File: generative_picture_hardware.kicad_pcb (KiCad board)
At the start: 2 copper layers, 100 x 100 mm, 64 parts, among them J1 e_Paper_HAT, J2 Conn_ARM_JTAG_SWD_10, J3 USB_C_Receptacle_USB2.0, Q1 PMN48XP, Q2 DMG9926UDM, Q3 MBT3904DW1, SW1 SW_Push, SW2 SW_Push, U1 AP2112K-3.3, U2 ESP32-WROOM-32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

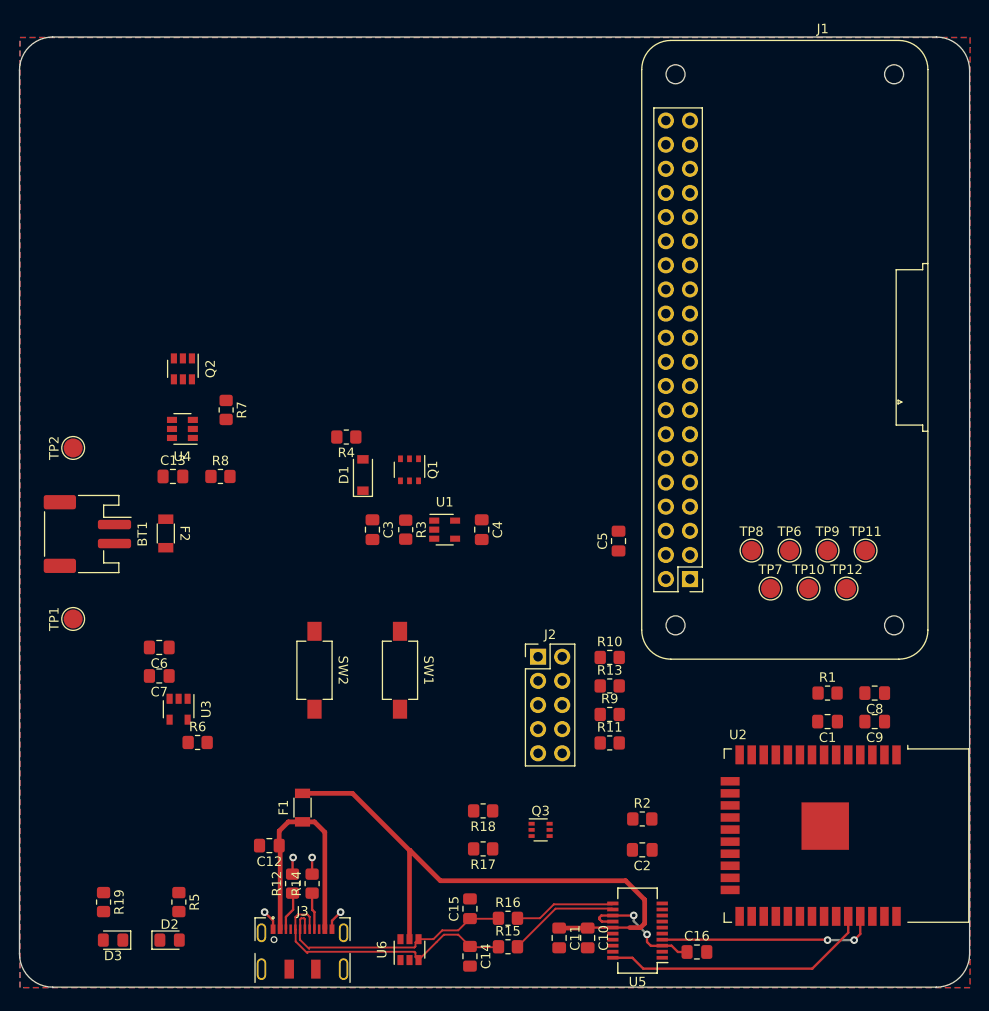
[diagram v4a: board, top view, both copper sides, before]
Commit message: Reroutes battery charging, protection and regulator
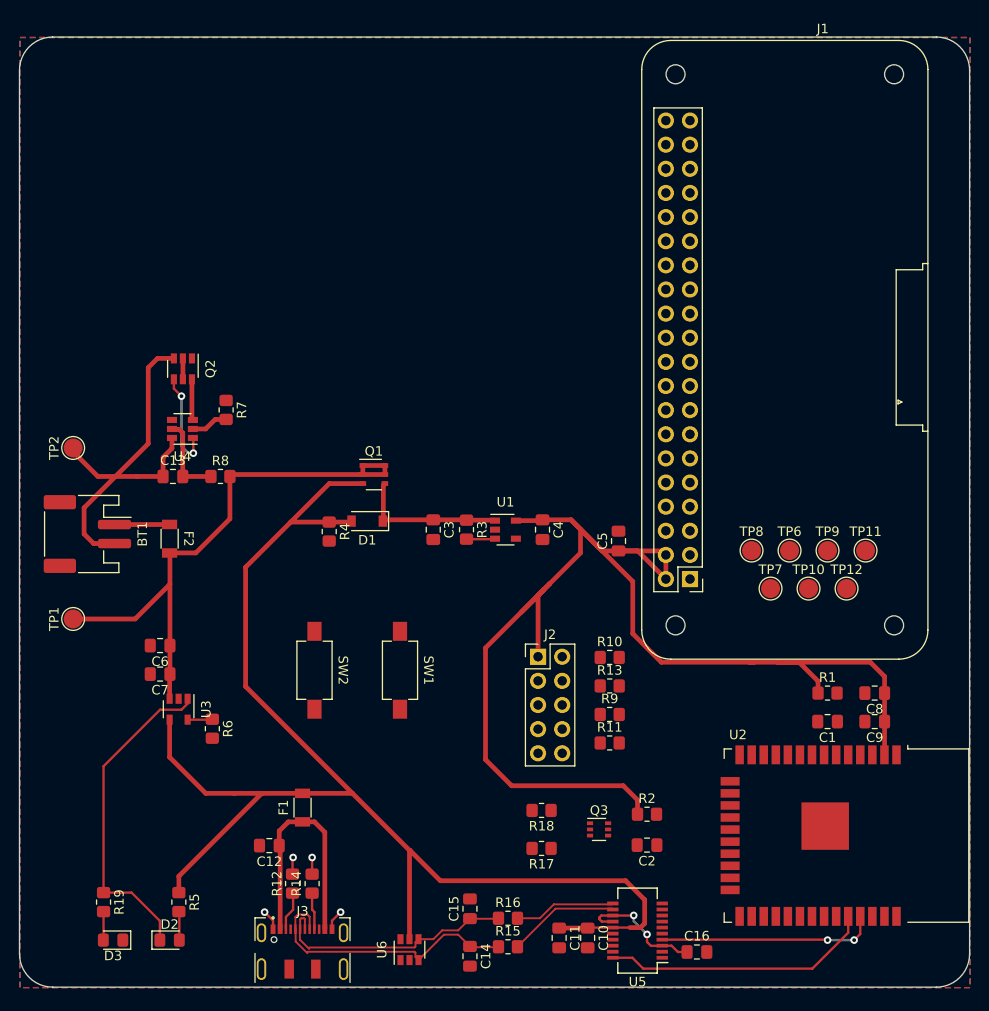
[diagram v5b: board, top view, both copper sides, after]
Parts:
- moved R4 10.1 mm to (132.6, 104.0), turned to -90 degrees
- moved C3 6.40 mm to (143.5, 103.8)
- moved C4 6.40 mm to (155.0, 103.8)
- moved R3 6.40 mm to (147.0, 103.8)
- moved U1 6.40 mm to (151.1, 103.8)
- moved R17 6.15 mm to (154.9, 137.3)
- moved R18 6.15 mm to (154.9, 133.3)
- moved Q3 6.15 mm to (160.9, 135.3)
- moved D1 4.87 mm to (136.6, 102.9), turned to 180 degrees
- moved Q1 3.78 mm to (137.2, 98.0), turned to 0 degrees
- moved R6 2.12 mm to (120.2, 124.8), turned to -90 degrees
- moved C2 0.71 mm to (166.0, 137.0)
- moved R2 0.71 mm to (166.0, 133.8)
- moved F2 0.68 mm to (115.8, 104.8)
- moved C6 0.22 mm to (114.8, 116.0)
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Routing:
- net +3V3: track 0.00 -> 144.1 mm
- net +5V: track 61.8 -> 146.4 mm
- net +BATT: track 0.00 -> 60.3 mm
- net Net-(BT1-Pad2): track 0.00 -> 42.4 mm
- net Net-(D2-Pad1): track 0.00 -> 34.6 mm
- net VCC: track 0.00 -> 15.9 mm
- net Net-(Q2-Pad4): track 0.00 -> 10.5 mm, vias 0 -> 2
- net Net-(C13-Pad2): track 0.00 -> 8.85 mm
- net Net-(BT1-Pad1): track 0.00 -> 5.80 mm
- net Net-(Q2-Pad6): track 0.00 -> 4.32 mm
- net Net-(R7-Pad2): track 0.00 -> 3.91 mm
- net Net-(D2-Pad2): track 0.00 -> 3.02 mm
- net Net-(R3-Pad2): track 0.00 -> 3.02 mm
- net Net-(D3-Pad2): track 0.00 -> 3.01 mm
- net Net-(R6-Pad1): track 0.00 -> 2.62 mm
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
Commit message: Reroutes the components that were left (except for GND)
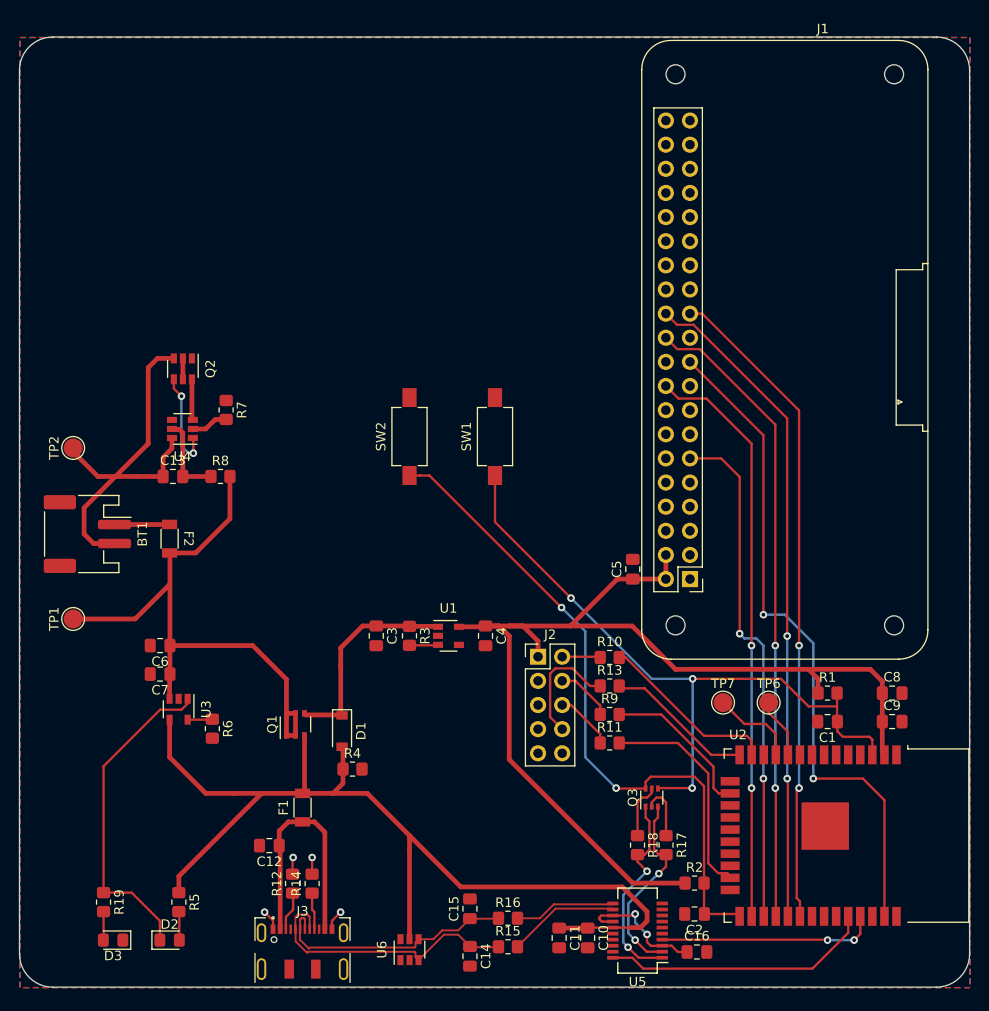
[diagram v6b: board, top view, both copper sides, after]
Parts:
- removed TP10: IO33, TestPoint:TestPoint_Pad_D2.0mm
- removed TP11: IO34, TestPoint:TestPoint_Pad_D2.0mm
- removed TP12: IO35, TestPoint:TestPoint_Pad_D2.0mm
- removed TP8: IO27, TestPoint:TestPoint_Pad_D2.0mm
- removed TP9: IO32, TestPoint:TestPoint_Pad_D2.0mm
- moved Q1 27.6 mm to (129.0, 124.3), turned to 90 degrees
- moved SW1 26.6 mm to (150.0, 94.0), turned to 90 degrees
- moved SW2 26.6 mm to (141.0, 94.0), turned to 90 degrees
- moved R4 25.1 mm to (135.0, 129.0), turned to 0 degrees
- moved D1 22.3 mm to (133.9, 125.0), turned to -90 degrees
- moved TP6 16.2 mm to (178.8, 122.0)
- moved R17 13.1 mm to (168.0, 137.0), turned to -90 degrees
- moved TP7 13.0 mm to (174.0, 122.0)
- moved C3 12.7 mm to (137.5, 115.0)
- moved C4 12.7 mm to (149.0, 115.0)
- moved R3 12.7 mm to (141.0, 115.0)
- moved U1 12.7 mm to (145.1, 115.0)
- moved R18 10.7 mm to (165.0, 137.0), turned to -90 degrees
- moved C2 8.81 mm to (171.0, 144.2)
- moved R2 8.81 mm to (171.0, 141.0)
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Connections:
- U2 pad 12: Net-(TP8-Pad1) -> unconnected-(U2-Pad12)
- U2 pad 6: Net-(TP11-Pad1) -> unconnected-(U2-Pad6)
- U2 pad 7: Net-(TP12-Pad1) -> unconnected-(U2-Pad7)
- U2 pad 8: Net-(TP9-Pad1) -> unconnected-(U2-Pad8)
- U2 pad 9: Net-(TP10-Pad1) -> unconnected-(U2-Pad9)
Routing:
- net ESP_EN: track 0.00 -> 73.8 mm, vias 0 -> 3
- net EPD_DIN: track 0.00 -> 71.2 mm, vias 0 -> 2
- net ESP_BOOT: track 0.00 -> 71.0 mm, vias 0 -> 2
- net EPD_CS: track 0.00 -> 69.8 mm, vias 0 -> 2
- net EPD_CLK: track 0.00 -> 69.2 mm, vias 0 -> 2
- net EPD_DC: track 0.00 -> 67.1 mm, vias 0 -> 2
- net EPD_BUSY: track 0.00 -> 61.3 mm, vias 0 -> 2
- net EPD_RST: track 0.00 -> 54.1 mm, vias 0 -> 2
- net +5V: track 146.4 -> 108.2 mm
- net +3V3: track 144.1 -> 116.7 mm
- net MTDO: track 0.00 -> 23.2 mm
- net DTR: track 0.00 -> 21.6 mm, vias 0 -> 2
- net RTS: track 0.00 -> 20.5 mm, vias 0 -> 2
- net MTMS: track 0.00 -> 19.1 mm
- net MTCK: track 0.00 -> 16.4 mm
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
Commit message: Routes all GND without relying on front copper fill
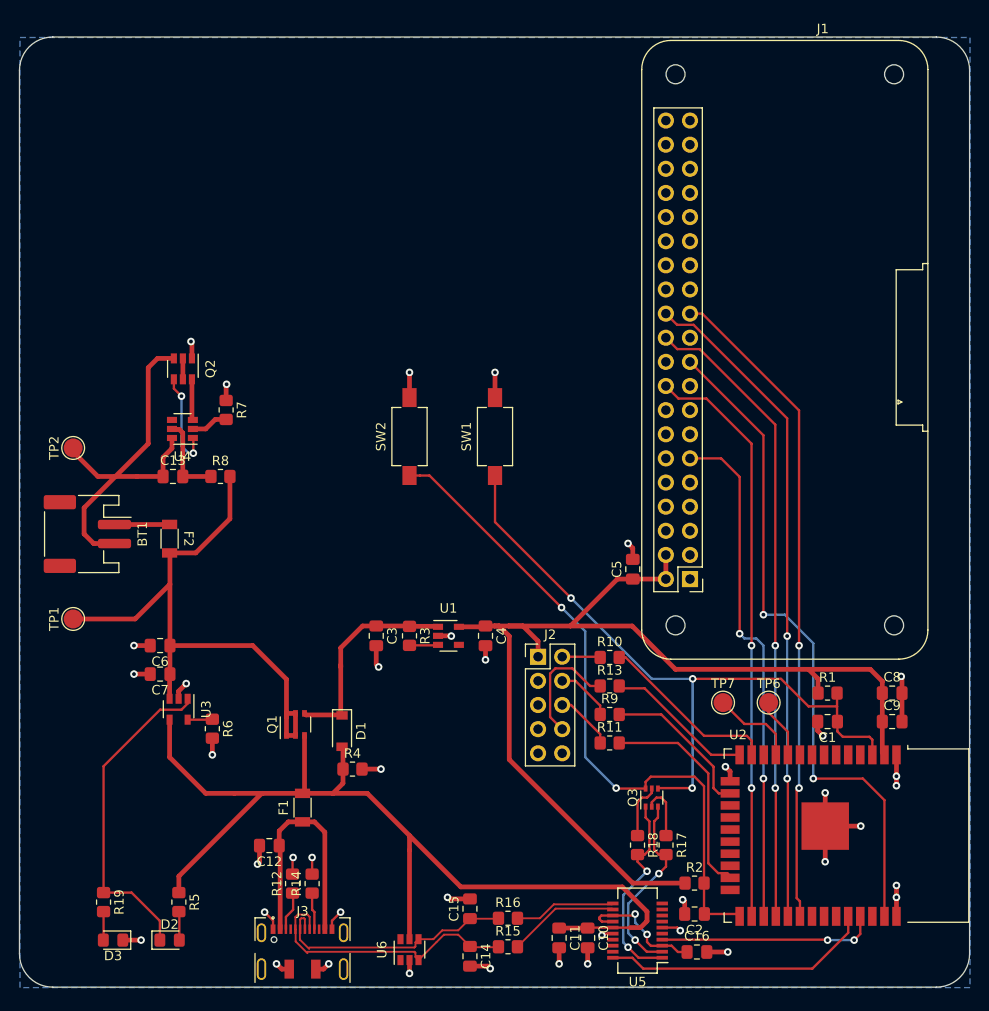
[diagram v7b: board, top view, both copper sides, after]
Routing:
- net GND: track 7.86 -> 82.3 mm, vias 4 -> 40
- removed copper zone on F.Cu, net GND
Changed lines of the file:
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@@
   (segment (start 115.74 103.26) (end 115.75 103.25) (width 0.5) (layer "F.Cu") (net 2))
   (segment (start 109.95 103.26) (end 115.74 103.26) (width 0.5) (layer "F.Cu") (net 2))
+  (segment (start 121.7 88.55) (end 121.75 88.5) (width 0.5) (layer "F.Cu") (net 3))
+  (segment (start 172.2875 148.25) (end 174.5 148.25) (width 0.5) (layer "F.Cu") (net 3))
+  (segment (start 192.255 141.255) (end 192.255 144.499748) (width 0.5) (layer "F.Cu") (net 3))
+  (segment (start 169.9625 142.9625) (end 169.75 142.75) (width 0.5) (layer "F.Cu") (net 3))
+  (segment (start 183.9625 124.9625) (end 184.5 125.5) (width 0.5) (layer "F.Cu") (net 3))
+  (segment (start 192.255 130.745) (end 192.255 127.499748) (width 0.5) (layer "F.Cu") (net 3))
+  (segment (start 184.755 134.999748) (end 184.755 138.745) (width 0.5) (layer "F.Cu") (net 3))
+  (segment (start 159.75 147.8075) (end 159.75 149.5) (width 0.5) (layer "F.Cu") (net 3))
+  (segment (start 188.499748 134.999748) (end 188.5 135) (width 0.5) (layer "F.Cu") (net 3))
   (segment (start 126.64 144.944098) (end 125.75 144.054098) (width 0.25) (layer "F.Cu") (net 3))
+  (segment (start 156.75 147.8075) (end 156.75 149.5) (width 0.5) (layer "F.Cu") (net 3))
   (segment (start 128.6925 138.361598) (end 128.75 138.304098) (width 0.25) (layer "F.Cu") (net 3))
   (segment (start 130.75 140.054098) (end 130.75 138.304098) (width 0.25) (layer "F.Cu") (net 3))
+  (segment (start 131.14 150.051598) (end 131.948402 150.051598) (width 0.5) (layer "F.Cu") (net 3))
+  (segment (start 141 89.9) (end 141 87.25) (width 0.5) (layer "F.Cu") (net 3))
+  (segment (start 150 89.9) (end 150 87.25) (width 0.5) (layer "F.Cu") (net 3))
+  (segment (start 164.5 106.925) (end 164.5 105.75) (width 0.5) (layer "F.Cu") (net 3))
+  (segment (start 162.4 146.3175) (end 161.4325 146.3175) (width 0.25) (layer "F.Cu") (net 3))
+  (segment (start 184.755 138.745) (end 184.75 138.75) (width 0.5) (layer "F.Cu") (net 3))
+  (segment (start 174.745 130.284748) (end 174.745 129.245) (width 0.5) (layer "F.Cu") (net 3))
+  (segment (start 127.551598 150.051598) (end 127 149.5) (width 0.5) (layer "F.Cu") (net 3))
+  (segment (start 147.3625 149.7375) (end 149.2375 149.7375) (width 0.5) (layer "F.Cu") (net 3))
+  (segment (start 169.9625 144.25) (end 169.9625 142.9625) (width 0.5) (layer "F.Cu") (net 3))
+  (segment (start 137.5 116.0125) (end 137.5 118) (width 0.5) (layer "F.Cu") (net 3))
+  (segment (start 118.1 85.775) (end 118.1 84.1) (width 0.5) (layer "F.Cu") (net 3))
+  (segment (start 147.3625 142.6625) (end 145.1625 142.6625) (width 0.5) (layer "F.Cu") (net 3))
+  (segment (start 110.825 147) (end 112.75 147) (width 0.5) (layer "F.Cu") (net 3))
+  (segment (start 131.948402 150.051598) (end 132.5 149.5) (width 0.5) (layer "F.Cu") (net 3))
+  (segment (start 169.1825 145.6825) (end 169.5 146) (width 0.25) (layer "F.Cu") (net 3))
+  (segment (start 145.4 115) (end 145.375 114.975) (width 0.5) (layer "F.Cu") (net 3))
+  (segment (start 136 129) (end 138 129) (width 0.5) (layer "F.Cu") (net 3))
+  (segment (start 141 149.102479) (end 141 150.5) (width 0.5) (layer "F.Cu") (net 3))
+  (segment (start 137.5 118) (end 137.75 118.25) (width 0.5) (layer "F.Cu") (net 3))
+  (segment (start 192.75 119.25) (end 192.8375 119.3375) (width 0.5) (layer "F.Cu") (net 3))
+  (segment (start 116.7 120.8) (end 117.5 120) (width 0.5) (layer "F.Cu") (net 3))
   (segment (start 132.84 144.964098) (end 133.75 144.054098) (width 0.25) (layer "F.Cu") (net 3))
+  (segment (start 121.7 90.2) (end 121.7 88.55) (width 0.5) (layer "F.Cu") (net 3))
+  (segment (start 125.2125 138.7875) (end 125 139) (width 0.5) (layer "F.Cu") (net 3))
+  (segment (start 128.34 150.051598) (end 127.551598 150.051598) (width 0.5) (layer "F.Cu") (net 3))
+  (segment (start 145.1625 142.6625) (end 145 142.5) (width 0.5) (layer "F.Cu") (net 3))
+  (segment (start 192.25 141.25) (end 192.255 141.255) (width 0.5) (layer "F.Cu") (net 3))
+  (segment (start 174.745 129.245) (end 174.25 128.75) (width 0.5) (layer "F.Cu") (net 3))
+  (segment (start 184.755 131.505) (end 184.75 131.5) (width 0.5) (layer "F.Cu") (net 3))
+  (segment (start 192.25 130.75) (end 192.255 130.745) (width 0.5) (layer "F.Cu") (net 3))
   (segment (start 132.84 145.851598) (end 132.84 144.964098) (width 0.25) (layer "F.Cu") (net 3))
+  (segment (start 113.7125 119) (end 112 119) (width 0.5) (layer "F.Cu") (net 3))
   (segment (start 126.64 145.851598) (end 126.64 144.944098) (width 0.25) (layer "F.Cu") (net 3))
+  (segment (start 116.7 121.6) (end 116.7 120.8) (width 0.5) (layer "F.Cu") (net 3))
+  (segment (start 192.8375 124) (end 192.8375 121) (width 0.5) (layer "F.Cu") (net 3))
+  (segment (start 183.9625 124) (end 183.9625 124.9625) (width 0.5) (layer "F.Cu") (net 3))
+  (segment (start 184.755 134.999748) (end 188.499748 134.999748) (width 0.5) (layer "F.Cu") (net 3))
+  (segment (start 118.1 84.1) (end 118 84) (width 0.5) (layer "F.Cu") (net 3))
+  (segment (start 149.2375 149.7375) (end 149.5 150) (width 0.5) (layer "F.Cu") (net 3))
+  (segment (start 145.375 114.975) (end 144 114.975) (width 0.5) (layer "F.Cu") (net 3))
+  (segment (start 120.25 125.75) (end 120.25 127.5) (width 0.5) (layer "F.Cu") (net 3))
+  (segment (start 161.4325 146.3175) (end 161.25 146.5) (width 0.25) (layer "F.Cu") (net 3))
   (segment (start 128.6925 140.054098) (end 128.6925 138.361598) (width 0.25) (layer "F.Cu") (net 3))
+  (segment (start 164.5 105.75) (end 164 105.25) (width 0.5) (layer "F.Cu") (net 3))
+  (segment (start 149 116.0125) (end 149 117.5) (width 0.5) (layer "F.Cu") (net 3))
+  (segment (start 192.8375 119.3375) (end 192.8375 121) (width 0.5) (layer "F.Cu") (net 3))
+  (segment (start 184.755 134.999748) (end 184.755 131.505) (width 0.5) (layer "F.Cu") (net 3))
+  (segment (start 113.7125 116) (end 112 116) (width 0.5) (layer "F.Cu") (net 3))
+  (segment (start 167.6 145.6825) (end 169.1825 145.6825) (width 0.25) (layer "F.Cu") (net 3))
+  (segment (start 125.2125 137.054098) (end 125.2125 138.7875) (width 0.5) (layer "F.Cu") (net 3))
+  (via (at 164 105.25) (size 0.8) (drill 0.4) (layers "F.Cu" "B.Cu") (net 3))
+  (via (at 117.5 120) (size 0.8) (drill 0.4) (layers "F.Cu" "B.Cu") (net 3))
+  (via (at 184.5 125.5) (size 0.8) (drill 0.4) (layers "F.Cu" "B.Cu") (net 3))
+  (via (at 118 84) (size 0.8) (drill 0.4) (layers "F.Cu" "B.Cu") (net 3))
+  (via (at 156.75 149.5) (size 0.8) (drill 0.4) (layers "F.Cu" "B.Cu") (net 3))
+  (via (at 112 116) (size 0.8) (drill 0.4) (layers "F.Cu" "B.Cu") (net 3))
+  (via (at 120.25 127.5) (size 0.8) (drill 0.4) (layers "F.Cu" "B.Cu") (net 3))
+  (via (at 145.4 115) (size 0.8) (drill 0.4) (layers "F.Cu" "B.Cu") (net 3))
   (via (at 130.75 138.304098) (size 0.8) (drill 0.4) (layers "F.Cu" "B.Cu") (net 3))
   (via (at 128.75 138.304098) (size 0.8) (drill 0.4) (layers "F.Cu" "B.Cu") (net 3))
+  (via (at 132.5 149.5) (size 0.8) (drill 0.4) (layers "F.Cu" "B.Cu") (net 3))
+  (via (at 127 149.5) (size 0.8) (drill 0.4) (layers "F.Cu" "B.Cu") (net 3))
   (via (at 133.75 144.054098) (size 0.8) (drill 0.4) (layers "F.Cu" "B.Cu") (net 3))
+  (via (at 150 87.25) (size 0.8) (drill 0.4) (layers "F.Cu" "B.Cu") (net 3))
+  (via (at 149 117.5) (size 0.8) (drill 0.4) (layers "F.Cu" "B.Cu") (net 3))
+  (via (at 192.75 119.25) (size 0.8) (drill 0.4) (layers "F.Cu" "B.Cu") (net 3))
+  (via (at 141 87.25) (size 0.8) (drill 0.4) (layers "F.Cu" "B.Cu") (net 3))
+  (via (at 121.75 88.5) (size 0.8) (drill 0.4) (layers "F.Cu" "B.Cu") (net 3))
+  (via (at 184.75 131.5) (size 0.8) (drill 0.4) (layers "F.Cu" "B.Cu") (net 3))
+  (via (at 137.75 118.25) (size 0.8) (drill 0.4) (layers "F.Cu" "B.Cu") (net 3))
+  (via (at 141 150.5) (size 0.8) (drill 0.4) (layers "F.Cu" "B.Cu") (net 3))
+  (via (at 192.25 130.75) (size 0.8) (drill 0.4) (layers "F.Cu" "B.Cu") (net 3))
+  (via (at 149.5 150) (size 0.8) (drill 0.4) (layers "F.Cu" "B.Cu") (net 3))
+  (via (at 159.75 149.5) (size 0.8) (drill 0.4) (layers "F.Cu" "B.Cu") (net 3))
+  (via (at 112.75 147) (size 0.8) (drill 0.4) (layers "F.Cu" "B.Cu") (net 3))
+  (via (at 138 129) (size 0.8) (drill 0.4) (layers "F.Cu" "B.Cu") (net 3))
+  (via (at 145 142.5) (size 0.8) (drill 0.4) (layers "F.Cu" "B.Cu") (net 3))
+  (via (at 169.5 146) (size 0.8) (drill 0.4) (layers "F.Cu" "B.Cu") (net 3))
+  (via (at 112 119) (size 0.8) (drill 0.4) (layers "F.Cu" "B.Cu") (net 3))
+  (via (at 192.25 142.5) (size 0.8) (drill 0.4) (layers "F.Cu" "B.Cu") (net 3))
+  (via (at 125 139) (size 0.8) (drill 0.4) (layers "F.Cu" "B.Cu") (net 3))
+  (via (at 174.25 128.75) (size 0.8) (drill 0.4) (layers "F.Cu" "B.Cu") (net 3))
+  (via (at 192.25 141.25) (size 0.8) (drill 0.4) (layers "F.Cu" "B.Cu") (net 3))
+  (via (at 188.5 135) (size 0.8) (drill 0.4) (layers "F.Cu" "B.Cu") (net 3))
+  (via (at 192.25 129.75) (size 0.8) (drill 0.4) (layers "F.Cu" "B.Cu") (net 3))
   (via (at 125.75 144.054098) (size 0.8) (drill 0.4) (layers "F.Cu" "B.Cu") (net 3))
+  (via (at 184.75 138.75) (size 0.8) (drill 0.4) (layers "F.Cu" "B.Cu") (net 3))
+  (via (at 169.75 142.75) (size 0.8) (drill 0.4) (layers "F.Cu" "B.Cu") (net 3))
+  (via (at 161.25 146.5) (size 0.8) (drill 0.4) (layers "F.Cu" "B.Cu") (net 3))
+  (via (at 174.5 148.25) (size 0.8) (drill 0.4) (layers "F.Cu" "B.Cu") (net 3))
   (segment (start 186 122.4) (end 186 123.9625) (width 0.25) (layer "F.Cu") (net 4))
   (segment (start 167.2 131) (end 167.15 131.05) (width 0.25) (layer "F.Cu") (net 4))
@@
       )
     )
-  )
-  (zone (net 3) (net_name "GND") (layer "F.Cu") (hatch edge 0.508)
-    (connect_pads (clearance 0.508))
-    (min_thickness 0.254) (filled_areas_thickness no)
-    (fill yes (thermal_gap 0.508) (thermal_bridge_width 0.508))
-    (polygon
-      (pts
-        (xy 200 152)
-        (xy 100 152)
-        (xy 100 52)
-        (xy 200 52)
-      )
-    )
